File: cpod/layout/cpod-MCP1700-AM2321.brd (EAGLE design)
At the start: 13 parts

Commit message: 布线完成
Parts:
- added IC1: PCF8563DIP, CEDT:DIL08
- added Y1: 32.768kHz, SparkFun-FreqCtrl:TC26H
- R3, R4: device SparkFun-Resistors:AXIAL-0.3 -> rcl:0207/2V
- moved I2C 5.68 mm to (41.9, -31.8), turned to 0 degrees
- moved R3 3.59 mm to (41.9, -35.6)
- moved R4 3.59 mm to (44.5, -35.6)
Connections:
- removed net D2: ARDUINO2.8
- new net INT0: ARDUINO2.8, IC1.3
- new net N$4: IC1.1, Y1.2
- new net N$6: IC1.2, Y1.1
- net GND: now also ARDUINO1.11, IC1.4; no longer ARDUINO2.9
- net SCL: now also IC1.6, R4.1; no longer R4.P$1
- net SDA: now also IC1.5, R3.1; no longer R3.P$1
- net VCC: now also IC1.8, R3.2, R4.2; no longer R3.P$2, R4.P$2
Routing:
- net SCL: track 13.8 -> 35.1 mm
- net SDA: track 11.2 -> 30.4 mm
- net MISO: track 34.1 -> 19.4 mm
- net INT0: track 0.00 -> 6.13 mm
- net MOSI: track 27.8 -> 32.3 mm
- net CSN: track 43.4 -> 39.6 mm
- net N$6: track 0.00 -> 2.54 mm
- net N$4: track 0.00 -> 2.54 mm
- net VCC: track 55.3 -> 57.9 mm
- net CE: track 33.8 -> 34.6 mm
- net SCK: track 20.2 -> 19.4 mm

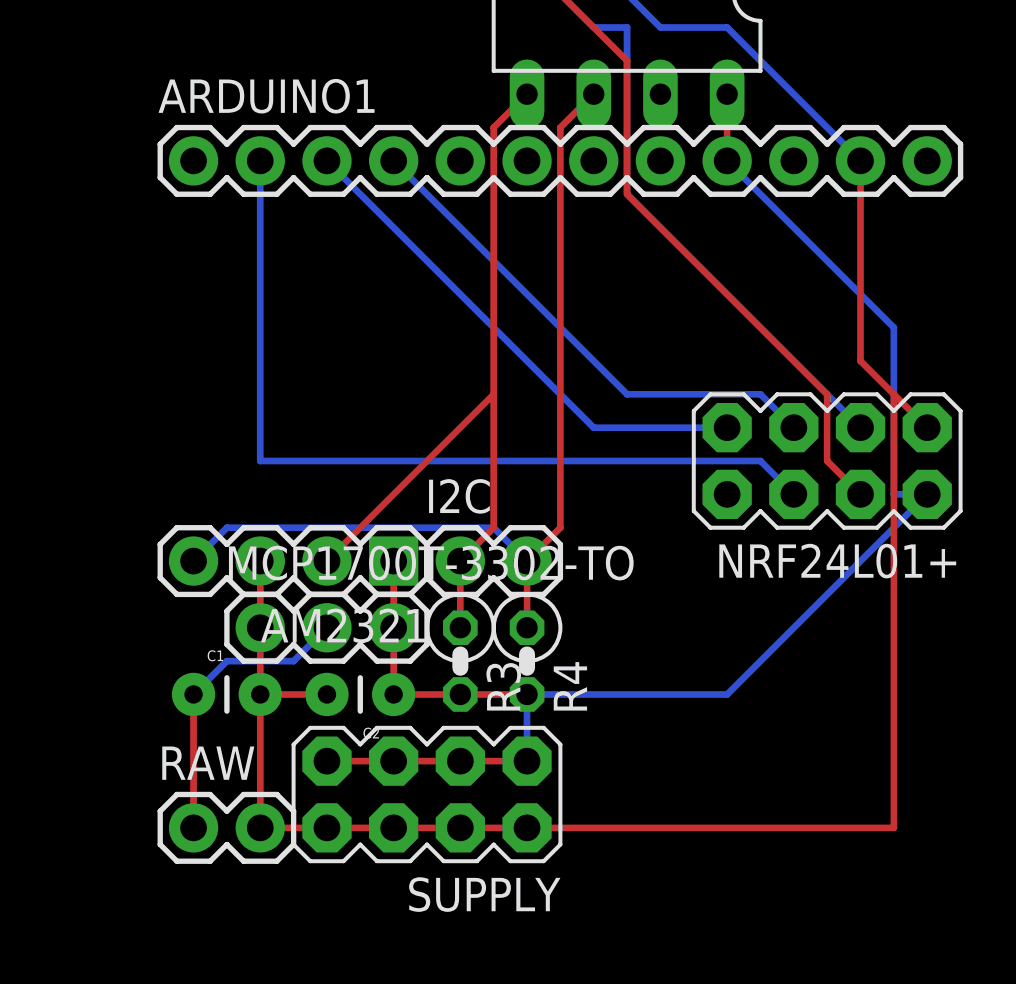
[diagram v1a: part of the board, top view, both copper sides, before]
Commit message: 去掉了SUPPLY
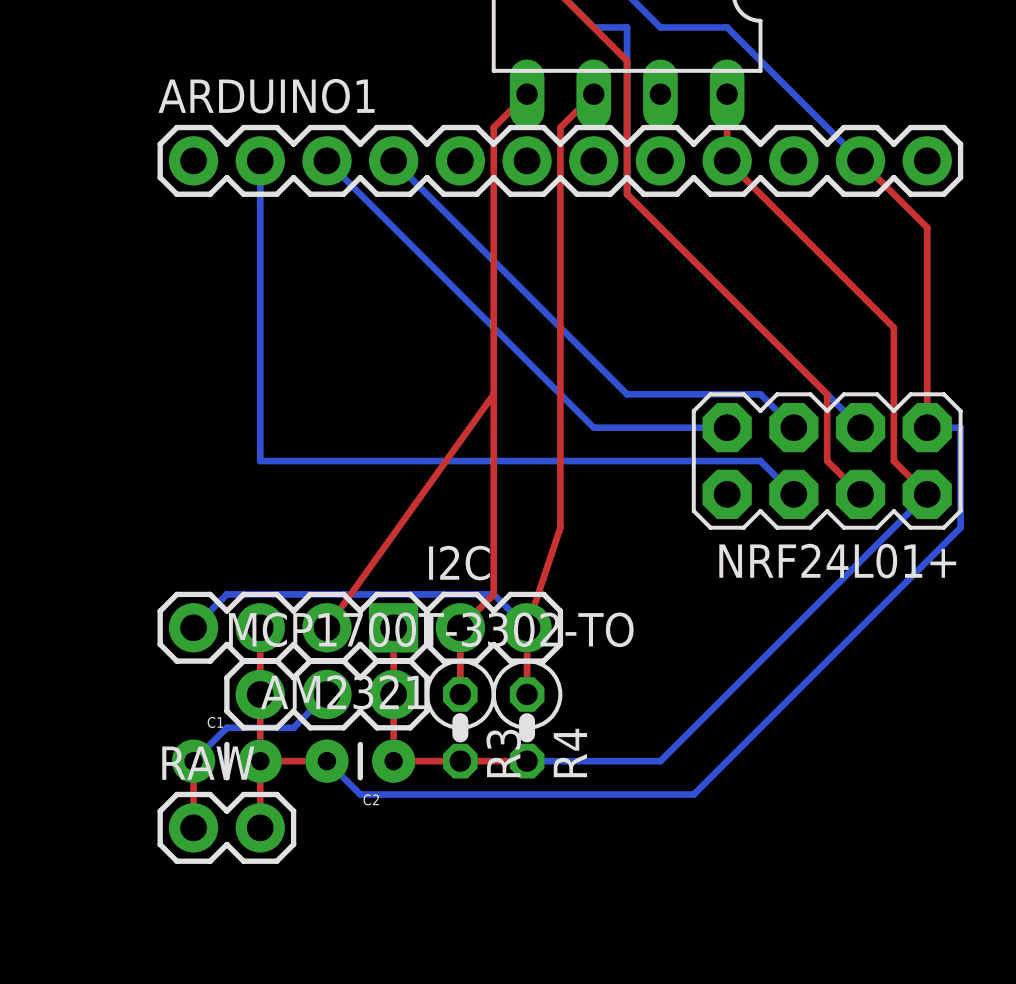
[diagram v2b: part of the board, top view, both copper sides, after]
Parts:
- removed SUPPLY: M04X2, SparkFun-Connectors:2X4
- moved AM2321 2.54 mm to (39.4, -34.3)
- moved C1 2.54 mm to (31.8, -39.4)
- moved C2 2.54 mm to (39.4, -39.4)
- moved I2C 2.54 mm to (41.9, -34.3)
- moved MCP1700T-3302-TO 2.54 mm to (34.3, -36.8)
- moved R3 2.54 mm to (41.9, -38.1)
- moved R4 2.54 mm to (44.5, -38.1)
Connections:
- net GND: no longer SUPPLY.2, SUPPLY.4, SUPPLY.6, SUPPLY.8
- net VCC: no longer SUPPLY.1, SUPPLY.3, SUPPLY.5, SUPPLY.7
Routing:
- net VCC: track 57.9 -> 48.0 mm
- net GND: track 81.5 -> 72.2 mm
- net SDA: track 30.4 -> 34.8 mm
- net RAW: track 11.2 -> 8.67 mm
- net SCL: track 35.1 -> 37.3 mm
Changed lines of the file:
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@@
 <wire x1="60.96" y1="-43.18" x2="0" y2="-43.18" width="0.4064" layer="41"/>
 <wire x1="0" y1="-43.18" x2="0" y2="0" width="0.4064" layer="41"/>
+<rectangle x1="50.8" y1="-43.18" x2="60.96" y2="-30.48" layer="41"/>
 </plain>
 <attributes>
@@
 </autorouter>
 <elements>
-<element name="AM2321" library="SparkFun-Connectors" package="1X04" value="" x="39.37" y="-31.75" rot="R180"/>
-<element name="MCP1700T-3302-TO" library="SparkFun-Connectors" package="1X03" value="" x="34.29" y="-34.29"/>
-<element name="C1" library="SparkFun-Capacitors" package="CAP-PTH-SMALL" value="1uF" x="31.75" y="-36.83"/>
-<element name="C2" library="SparkFun-Capacitors" package="CAP-PTH-SMALL" value="1uF" x="39.37" y="-36.83" rot="R180"/>
+<element name="AM2321" library="SparkFun-Connectors" package="1X04" value="" x="39.37" y="-34.29" rot="R180"/>
+<element name="MCP1700T-3302-TO" library="SparkFun-Connectors" package="1X03" value="" x="34.29" y="-36.83"/>
+<element name="C1" library="SparkFun-Capacitors" package="CAP-PTH-SMALL" value="1uF" x="31.75" y="-39.37"/>
+<element name="C2" library="SparkFun-Capacitors" package="CAP-PTH-SMALL" value="1uF" x="39.37" y="-39.37" rot="R180"/>
 <element name="ARDUINO1" library="SparkFun-Connectors" package="1X12" value="M12PTH" x="31.75" y="-16.51"/>
 <element name="ARDUINO2" library="SparkFun-Connectors" package="1X12" value="M12PTH" x="31.75" y="-1.27"/>
 <element name="RAW" library="SparkFun-Connectors" package="1X02" value="" x="31.75" y="-41.91"/>
 <element name="NRF24L01+" library="SparkFun-Connectors" package="2X4" value="M04X2" x="55.88" y="-27.94" rot="R180"/>
-<element name="R3" library="rcl" package="0207/2V" value="4.7k" x="41.91" y="-35.56" rot="R270"/>
-<element name="R4" library="rcl" package="0207/2V" value="4.7k" x="44.45" y="-35.56" rot="R270"/>
-<element name="I2C" library="SparkFun-Connectors" package="1X02" value="" x="41.91" y="-31.75"/>
+<element name="R3" library="rcl" package="0207/2V" value="4.7k" x="41.91" y="-38.1" rot="R270"/>
+<element name="R4" library="rcl" package="0207/2V" value="4.7k" x="44.45" y="-38.1" rot="R270"/>
+<element name="I2C" library="SparkFun-Connectors" package="1X02" value="" x="41.91" y="-34.29"/>
 <element name="U$2" library="SparkFun-Aesthetics" package="OSHW-LOGO-L" value="" x="5.08" y="-38.1"/>
 <element name="IC1" library="CEDT" package="DIL08" value="PCF8563DIP" x="48.26" y="-10.16" rot="R180"/>
 <element name="Y1" library="SparkFun-FreqCtrl" package="TC26H" value="32.768kHz" x="50.8" y="-3.81"/>
-<element name="SUPPLY" library="SparkFun-Connectors" package="2X4" value="M04X2" x="40.64" y="-40.64" rot="R180"/>
 </elements>
 <signals>
@@
 <contactref element="R4" pad="1"/>
 <contactref element="IC1" pad="6"/>
-<wire x1="44.45" y1="-31.75" x2="44.45" y2="-34.29" width="0.254" layer="1"/>
+<wire x1="44.45" y1="-34.29" x2="44.45" y2="-36.83" width="0.254" layer="1"/>
 <wire x1="45.72" y1="-15.24" x2="46.99" y2="-13.97" width="0.254" layer="1"/>
 <wire x1="45.72" y1="-30.48" x2="45.72" y2="-15.24" width="0.254" layer="1"/>
-<wire x1="44.45" y1="-31.75" x2="45.72" y2="-30.48" width="0.254" layer="1"/>
-<wire x1="33.02" y1="-30.48" x2="31.75" y2="-31.75" width="0.254" layer="16"/>
-<wire x1="43.18" y1="-30.48" x2="33.02" y2="-30.48" width="0.254" layer="16"/>
-<wire x1="44.45" y1="-31.75" x2="43.18" y2="-30.48" width="0.254" layer="16"/>
+<wire x1="44.45" y1="-34.29" x2="45.72" y2="-30.48" width="0.254" layer="1"/>
+<wire x1="33.02" y1="-33.02" x2="31.75" y2="-34.29" width="0.254" layer="16"/>
+<wire x1="43.18" y1="-33.02" x2="33.02" y2="-33.02" width="0.254" layer="16"/>
+<wire x1="44.45" y1="-34.29" x2="43.18" y2="-33.02" width="0.254" layer="16"/>
 </signal>
 <signal name="GND">
@@
 <contactref element="NRF24L01+" pad="1"/>
 <contactref element="IC1" pad="4"/>
-<contactref element="SUPPLY" pad="2"/>
-<contactref element="SUPPLY" pad="8"/>
-<contactref element="SUPPLY" pad="6"/>
-<contactref element="SUPPLY" pad="4"/>
 <contactref element="ARDUINO1" pad="11"/>
-<wire x1="34.29" y1="-34.29" x2="34.29" y2="-36.83" width="0.254" layer="1"/>
-<wire x1="34.29" y1="-36.83" x2="36.83" y2="-36.83" width="0.254" layer="1"/>
-<wire x1="34.29" y1="-34.29" x2="34.29" y2="-31.75" width="0.254" layer="1"/>
-<wire x1="36.83" y1="-41.91" x2="34.29" y2="-41.91" width="0.254" layer="1"/>
-<wire x1="36.83" y1="-41.91" x2="39.37" y2="-41.91" width="0.254" layer="1"/>
-<wire x1="39.37" y1="-41.91" x2="41.91" y2="-41.91" width="0.254" layer="1"/>
-<wire x1="41.91" y1="-41.91" x2="44.45" y2="-41.91" width="0.254" layer="1"/>
-<wire x1="34.29" y1="-41.91" x2="34.29" y2="-36.83" width="0.254" layer="1"/>
+<wire x1="34.29" y1="-36.83" x2="34.29" y2="-39.37" width="0.254" layer="1"/>
+<wire x1="34.29" y1="-39.37" x2="36.83" y2="-39.37" width="0.254" layer="1"/>
+<wire x1="34.29" y1="-39.37" x2="34.29" y2="-41.91" width="0.254" layer="1"/>
+<wire x1="34.29" y1="-36.83" x2="34.29" y2="-34.29" width="0.254" layer="1"/>
 <wire x1="49.53" y1="-11.43" x2="44.45" y2="-6.35" width="0.254" layer="16"/>
 <wire x1="52.07" y1="-11.43" x2="49.53" y2="-11.43" width="0.254" layer="16"/>
 <wire x1="57.15" y1="-16.51" x2="52.07" y2="-11.43" width="0.254" layer="16"/>
-<wire x1="57.15" y1="-24.13" x2="58.42" y2="-25.4" width="0.254" layer="1"/>
-<wire x1="58.42" y1="-25.4" x2="59.69" y2="-26.67" width="0.254" layer="1"/>
-<wire x1="57.15" y1="-16.51" x2="57.15" y2="-24.13" width="0.254" layer="1"/>
-<wire x1="58.42" y1="-41.91" x2="44.45" y2="-41.91" width="0.254" layer="1"/>
-<wire x1="58.42" y1="-25.4" x2="58.42" y2="-41.91" width="0.254" layer="1"/>
+<wire x1="59.69" y1="-19.05" x2="59.69" y2="-26.67" width="0.254" layer="1"/>
+<wire x1="57.15" y1="-16.51" x2="59.69" y2="-19.05" width="0.254" layer="1"/>
+<wire x1="38.1" y1="-40.64" x2="36.83" y2="-39.37" width="0.254" layer="16"/>
+<wire x1="50.8" y1="-40.64" x2="38.1" y2="-40.64" width="0.254" layer="16"/>
+<wire x1="60.96" y1="-30.48" x2="50.8" y2="-40.64" width="0.254" layer="16"/>
+<wire x1="60.96" y1="-26.67" x2="60.96" y2="-30.48" width="0.254" layer="16"/>
+<wire x1="59.69" y1="-26.67" x2="60.96" y2="-26.67" width="0.254" layer="16"/>
 </signal>
 <signal name="SDA">
@@
 <contactref element="R3" pad="1"/>
 <contactref element="IC1" pad="5"/>
-<wire x1="41.91" y1="-31.75" x2="41.91" y2="-34.29" width="0.254" layer="1"/>
+<wire x1="41.91" y1="-34.29" x2="41.91" y2="-36.83" width="0.254" layer="1"/>
 <wire x1="43.18" y1="-15.24" x2="44.45" y2="-13.97" width="0.254" layer="1"/>
-<wire x1="43.18" y1="-30.48" x2="43.18" y2="-25.4" width="0.254" layer="1"/>
+<wire x1="43.18" y1="-33.02" x2="43.18" y2="-25.4" width="0.254" layer="1"/>
 <wire x1="43.18" y1="-25.4" x2="43.18" y2="-15.24" width="0.254" layer="1"/>
-<wire x1="41.91" y1="-31.75" x2="43.18" y2="-30.48" width="0.254" layer="1"/>
-<wire x1="43.18" y1="-25.4" x2="36.83" y2="-31.75" width="0.254" layer="1"/>
+<wire x1="41.91" y1="-34.29" x2="43.18" y2="-33.02" width="0.254" layer="1"/>
+<wire x1="43.18" y1="-25.4" x2="36.83" y2="-34.29" width="0.254" layer="1"/>
 </signal>
 <signal name="VCC">
@@
 <contactref element="MCP1700T-3302-TO" pad="3"/>
 <contactref element="IC1" pad="8"/>
-<contactref element="SUPPLY" pad="7"/>
-<contactref element="SUPPLY" pad="5"/>
-<contactref element="SUPPLY" pad="3"/>
-<contactref element="SUPPLY" pad="1"/>
-<wire x1="39.37" y1="-39.37" x2="36.83" y2="-39.37" width="0.254" layer="1"/>
+<wire x1="39.37" y1="-34.29" x2="39.37" y2="-36.83" width="0.254" layer="1"/>
+<wire x1="52.07" y1="-16.51" x2="52.07" y2="-13.97" width="0.254" layer="1"/>
 <wire x1="39.37" y1="-39.37" x2="41.91" y2="-39.37" width="0.254" layer="1"/>
 <wire x1="41.91" y1="-39.37" x2="44.45" y2="-39.37" width="0.254" layer="1"/>
-<wire x1="39.37" y1="-31.75" x2="39.37" y2="-34.29" width="0.254" layer="1"/>
-<wire x1="52.07" y1="-16.51" x2="52.07" y2="-13.97" width="0.254" layer="1"/>
-<wire x1="39.37" y1="-36.83" x2="41.91" y2="-36.83" width="0.254" layer="1"/>
-<wire x1="41.91" y1="-36.83" x2="44.45" y2="-36.83" width="0.254" layer="1"/>
-<wire x1="52.07" y1="-36.83" x2="59.69" y2="-29.21" width="0.254" layer="16"/>
-<wire x1="44.45" y1="-36.83" x2="52.07" y2="-36.83" width="0.254" layer="16"/>
-<wire x1="58.42" y1="-22.86" x2="52.07" y2="-16.51" width="0.254" layer="16"/>
-<wire x1="58.42" y1="-29.21" x2="58.42" y2="-22.86" width="0.254" layer="16"/>
-<wire x1="59.69" y1="-29.21" x2="58.42" y2="-29.21" width="0.254" layer="16"/>
-<wire x1="39.37" y1="-36.83" x2="39.37" y2="-34.29" width="0.254" layer="1"/>
-<wire x1="44.45" y1="-36.83" x2="44.45" y2="-39.37" width="0.254" layer="16"/>
+<wire x1="49.53" y1="-39.37" x2="59.69" y2="-29.21" width="0.254" layer="16"/>
+<wire x1="44.45" y1="-39.37" x2="49.53" y2="-39.37" width="0.254" layer="16"/>
+<wire x1="58.42" y1="-22.86" x2="52.07" y2="-16.51" width="0.254" layer="1"/>
+<wire x1="58.42" y1="-27.94" x2="58.42" y2="-22.86" width="0.254" layer="1"/>
+<wire x1="59.69" y1="-29.21" x2="58.42" y2="-27.94" width="0.254" layer="1"/>
+<wire x1="39.37" y1="-39.37" x2="39.37" y2="-36.83" width="0.254" layer="1"/>
 </signal>
 <signal name="RAW">
@@
 <contactref element="C1" pad="1"/>
 <contactref element="RAW" pad="1"/>
-<wire x1="31.75" y1="-41.91" x2="31.75" y2="-36.83" width="0.254" layer="1"/>
-<wire x1="35.56" y1="-35.56" x2="36.83" y2="-34.29" width="0.254" layer="16"/>
-<wire x1="33.02" y1="-35.56" x2="35.56" y2="-35.56" width="0.254" layer="16"/>
-<wire x1="31.75" y1="-36.83" x2="33.02" y2="-35.56" width="0.254" layer="16"/>
+<wire x1="31.75" y1="-41.91" x2="31.75" y2="-39.37" width="0.254" layer="1"/>
+<wire x1="35.56" y1="-38.1" x2="36.83" y2="-36.83" width="0.254" layer="16"/>
+<wire x1="33.02" y1="-38.1" x2="35.56" y2="-38.1" width="0.254" layer="16"/>
+<wire x1="31.75" y1="-39.37" x2="33.02" y2="-38.1" width="0.254" layer="16"/>
 </signal>
 <signal name="AD3">
